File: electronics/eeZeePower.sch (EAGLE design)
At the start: 10 parts

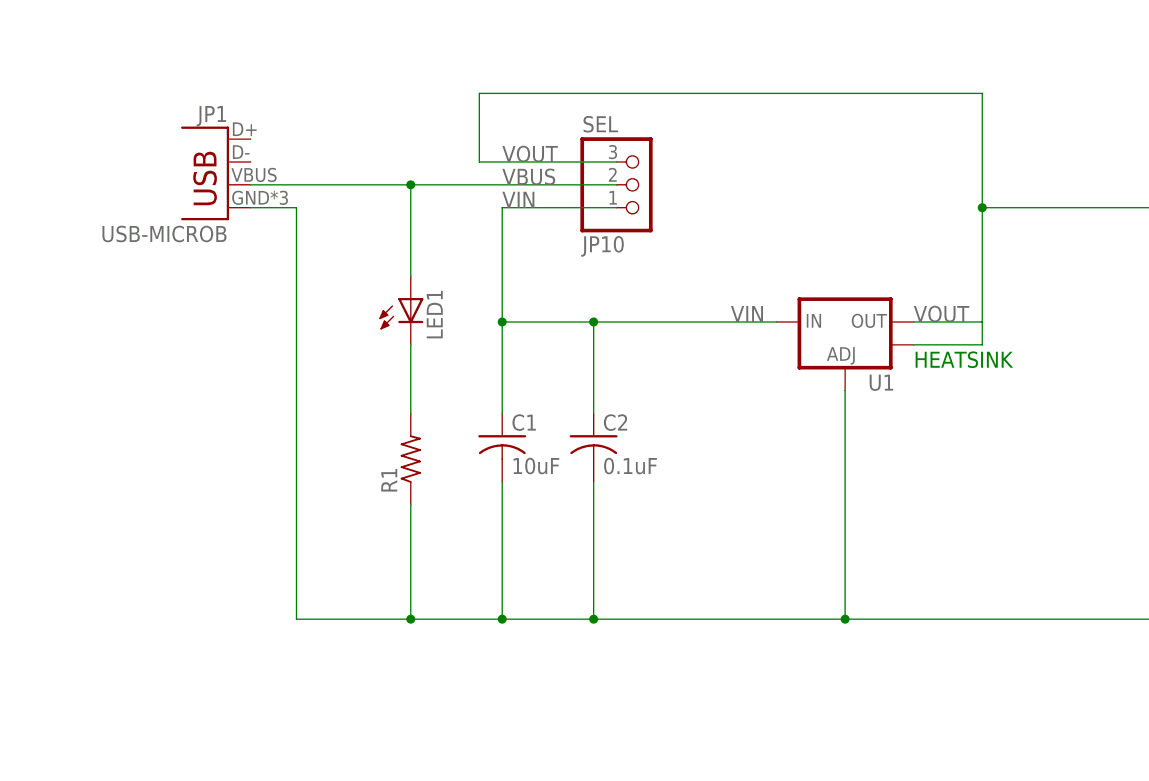
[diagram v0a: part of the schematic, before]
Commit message: updated microb footprint with new library version, added shielding to ground, fixed missing junction
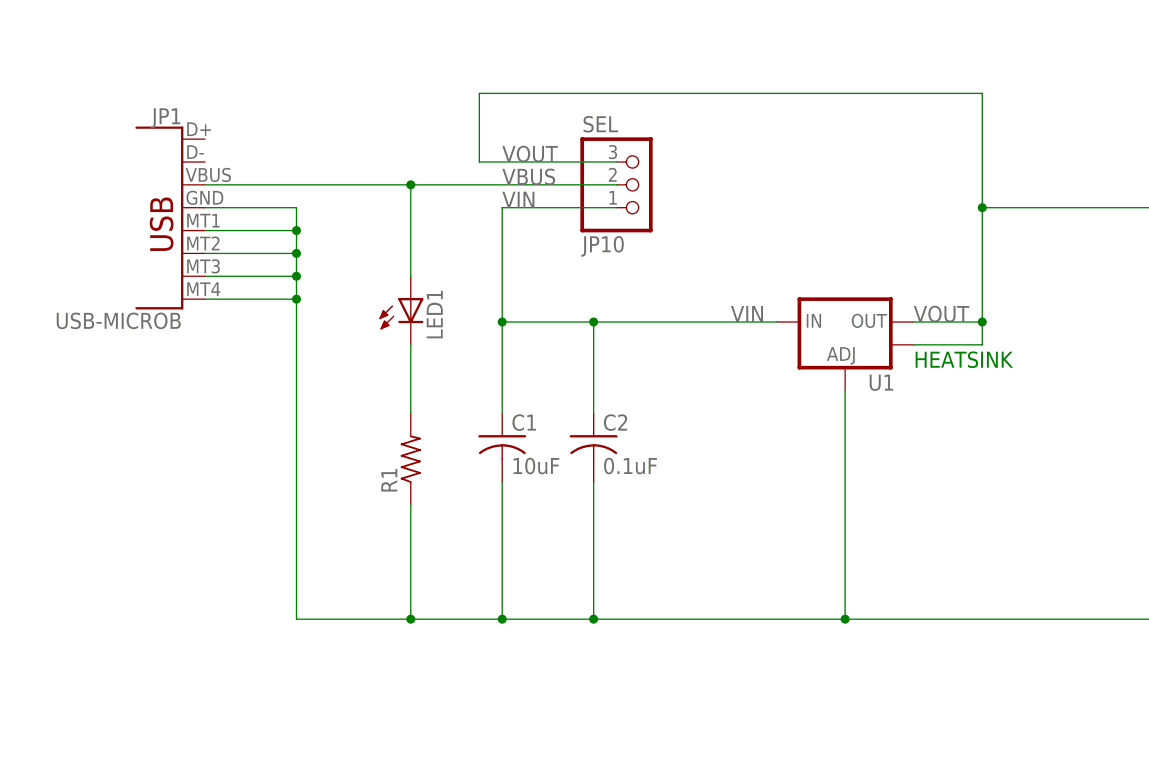
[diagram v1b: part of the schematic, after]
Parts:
- JP1: device SparkFun-Connectors:USB-MICROB -> bt_electromech:USB-MICROB
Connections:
- net GND: now also JP1.SHIELD1, JP1.SHIELD2, JP1.SHIELD3, JP1.SHIELD4
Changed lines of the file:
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@@
 <part name="JP3" library="pinhead-2" deviceset="PINHD-1X02" device="_2.54-S"/>
 <part name="JP4" library="pinhead-2" deviceset="PINHD-1X02" device="_2.54-S"/>
-<part name="JP1" library="SparkFun-Connectors" deviceset="USB" device="-MICROB"/>
+<part name="JP1" library="bt_electromech" deviceset="USB" device="-MICROB"/>
 </parts>
 <sheets>
@@
 <instance part="JP3" gate="A" x="182.88" y="114.3"/>
 <instance part="JP4" gate="A" x="182.88" y="129.54"/>
-<instance part="JP1" gate="G$1" x="53.34" y="116.84" rot="MR0"/>
+<instance part="JP1" gate="G$1" x="48.26" y="116.84" rot="MR0"/>
 </instances>
 <busses>
@@
 <wire x1="83.82" y1="71.12" x2="83.82" y2="86.36" width="0.1524" layer="91"/>
 <junction x="93.98" y="71.12"/>
-<wire x1="60.96" y1="71.12" x2="60.96" y2="116.84" width="0.1524" layer="91"/>
+<wire x1="60.96" y1="71.12" x2="60.96" y2="106.68" width="0.1524" layer="91"/>
+<wire x1="60.96" y1="106.68" x2="60.96" y2="109.22" width="0.1524" layer="91"/>
+<wire x1="60.96" y1="109.22" x2="60.96" y2="111.76" width="0.1524" layer="91"/>
+<wire x1="60.96" y1="111.76" x2="60.96" y2="114.3" width="0.1524" layer="91"/>
+<wire x1="60.96" y1="114.3" x2="60.96" y2="116.84" width="0.1524" layer="91"/>
 <wire x1="83.82" y1="71.12" x2="73.66" y2="71.12" width="0.1524" layer="91"/>
 <pinref part="R1" gate="G$1" pin="1"/>
@@
 <wire x1="121.92" y1="71.12" x2="160.02" y2="71.12" width="0.1524" layer="91"/>
 <pinref part="JP1" gate="G$1" pin="GND"/>
-<wire x1="55.88" y1="116.84" x2="60.96" y2="116.84" width="0.1524" layer="91"/>
+<wire x1="50.8" y1="116.84" x2="60.96" y2="116.84" width="0.1524" layer="91"/>
+<pinref part="JP1" gate="G$1" pin="SHIELD2"/>
+<wire x1="50.8" y1="111.76" x2="60.96" y2="111.76" width="0.1524" layer="91"/>
+<junction x="60.96" y="111.76"/>
+<pinref part="JP1" gate="G$1" pin="SHIELD3"/>
+<wire x1="50.8" y1="109.22" x2="60.96" y2="109.22" width="0.1524" layer="91"/>
+<junction x="60.96" y="109.22"/>
+<pinref part="JP1" gate="G$1" pin="SHIELD4"/>
+<wire x1="50.8" y1="106.68" x2="60.96" y2="106.68" width="0.1524" layer="91"/>
+<junction x="60.96" y="106.68"/>
+<pinref part="JP1" gate="G$1" pin="SHIELD1"/>
+<wire x1="50.8" y1="114.3" x2="60.96" y2="114.3" width="0.1524" layer="91"/>
+<junction x="60.96" y="114.3"/>
 </segment>
 </net>
@@
 <pinref part="U1" gate="G$1" pin="OUT@1"/>
 <wire x1="129.54" y1="101.6" x2="137.16" y2="101.6" width="0.1524" layer="91"/>
+<junction x="137.16" y="104.14"/>
 </segment>
 </net>
@@
 <label x="83.82" y="119.38" size="1.778" layer="95"/>
 <pinref part="JP1" gate="G$1" pin="VBUS"/>
-<wire x1="55.88" y1="119.38" x2="73.66" y2="119.38" width="0.1524" layer="91"/>
+<wire x1="50.8" y1="119.38" x2="73.66" y2="119.38" width="0.1524" layer="91"/>
 </segment>
 </net>

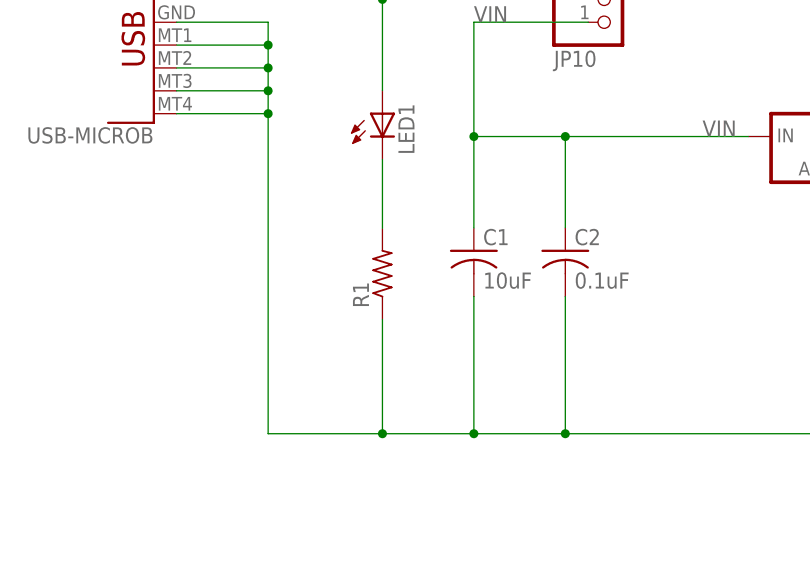
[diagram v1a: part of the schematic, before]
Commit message: added value to resistor, removed silk value
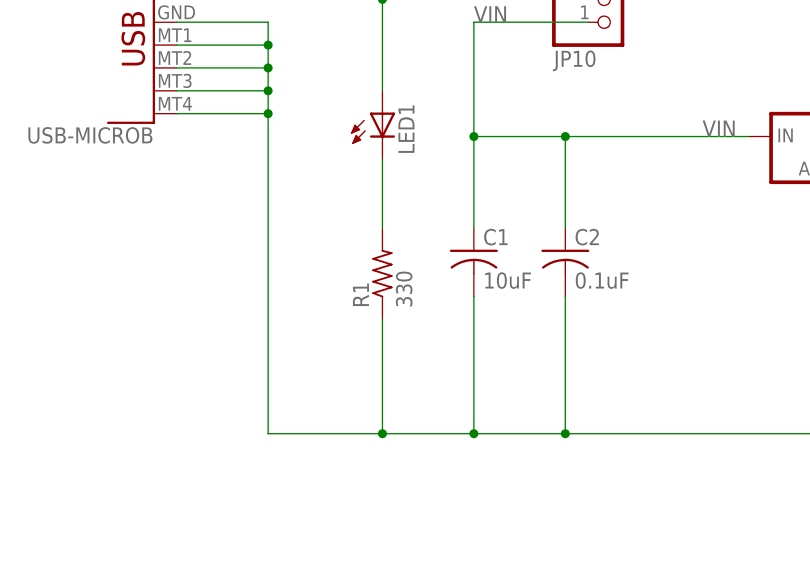
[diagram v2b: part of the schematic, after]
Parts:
- R1: value (none) -> 330
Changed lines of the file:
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@@
 <part name="C2" library="rcl" deviceset="C-US" device="C0603" value="0.1uF"/>
 <part name="C4" library="rcl" deviceset="CPOL-US" device="SMCB" value="100uF"/>
-<part name="R1" library="resistor" deviceset="R-US_" device="R0603"/>
+<part name="R1" library="resistor" deviceset="R-US_" device="R0603" value="330"/>
 <part name="C1" library="rcl" deviceset="C-US" device="C1206" value="10uF"/>
 <part name="FRAME1" library="mes" deviceset="LETTER_L" device=""/>
